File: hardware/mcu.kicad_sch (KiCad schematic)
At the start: 26 parts, among them SW1 BOOT / PTS810, SW2 RESET / PTS810, U2 ESP32-C6-MINI-1-H4, U4 BQ32000, Y1 32.768kHz

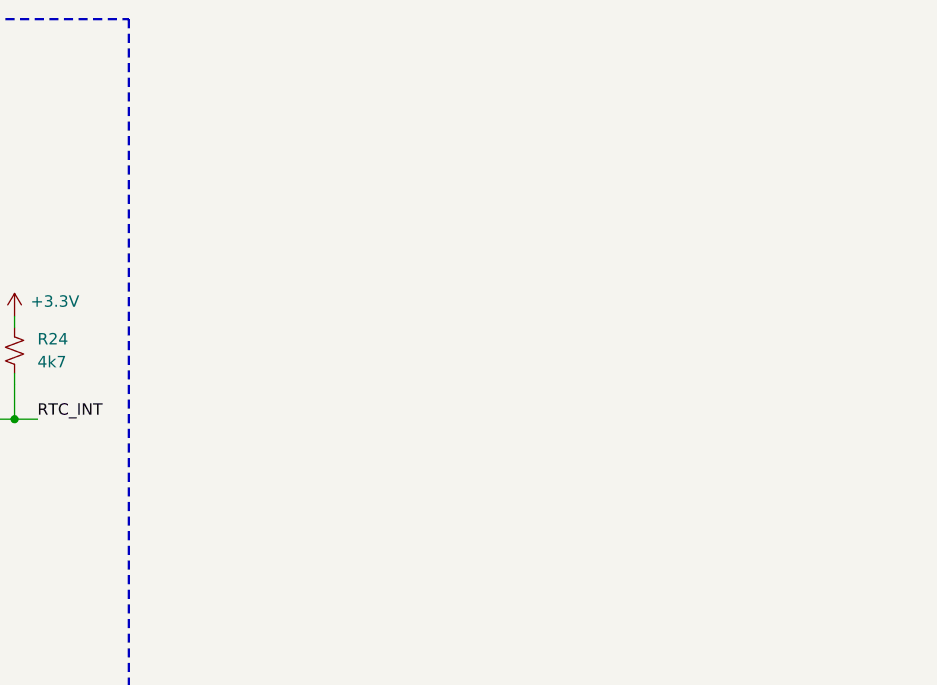
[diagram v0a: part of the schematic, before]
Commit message: hardware: I2C seviye dönüştürücüyü mcu'ya taşı, OUT_POS aktif deşarjı ekle (TASK-048/049/050)
- mcu: I2C seviye dönüştürücü (Q1, Q2, R4-R7) usb_pd_controller'dan
  taşındı; sayfa A4 -> A3. Bağlantı değişmedi.
- usb_pd_controller: R59 bleed yerine SW_EN kontrollü deşarj. Q4 BSS138P
  SW_EN'i ters çevirir, Q6 BSS138P OUT_POS'u R67 1k 2W 2512 üzerinden
  boşaltır; gate SW_OUT'tan R66 100k, D10 BZT52C12 ile 12 V. R59 10k 0805
  -> 100k 0603. Q1/Q2 alanları BSS138P,215 datasheet'ine göre düzeltildi.
- Karar: design_decisions/output/CIKIS_DESARJI_20260923.md; firmware
  deşarj bekleme ve dış kaynak uyarısı FIRMWARE_GEREKSINIMLERI.md §3.
- Backlog: TASK-048/049 Done, TASK-050 bring-up doğrulaması açıldı,
  TASK-006'ya footprint notu.

Kanıt: ERC 0/0. Netlist farkı yalnız beklenen netler: yeni DISCH_G
(D10.1, Q4.3, Q6.1, R66.2) ve Net-(Q6-D) (Q6.3, R67.2); SW_EN += Q4.1,
SW_OUT += R66.1, OUT_POS += R67.1, GND += D10.2, Q4.2, Q6.2.

Co-Authored-By: Claude Opus 5.5 <noreply@anthropic.com>
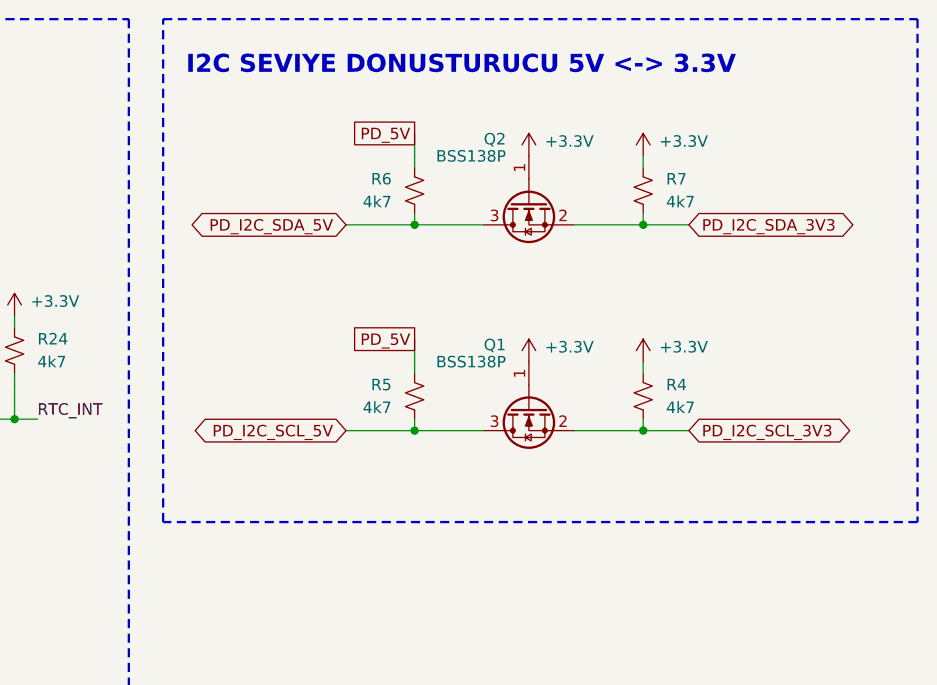
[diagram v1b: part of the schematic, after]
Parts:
- added Q1, Q2: BSS138P, Package_TO_SOT_SMD:SOT-23, symbol Transistor_FET:BSS138
- added R4, R5, R6, R7: 4k7, Resistor_SMD:R_0402_1005Metric, symbol Device:R_Small_US
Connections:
- net +3.3V: now also Q1.1 (G), Q2.1 (G), R4.2, R7.1
- net PD_I2C_SCL_3V3: now also Q1.2 (S), R4.1
- net PD_I2C_SDA_3V3: now also Q2.2 (S), R7.2
- new net PD_5V: R5.1, R6.1
- new net PD_I2C_SCL_5V: Q1.3 (D), R5.2
- new net PD_I2C_SDA_5V: Q2.3 (D), R6.2
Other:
- note added: "I2C SEVIYE DONUSTURUCU 5V <-> 3.3V"

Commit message: hardware: Ethernet mezanin blogu ve besleme anahtari (TASK-051/060)
Waveshare 2-CH UART TO ETH (CH9121) modulu mcu sayfasina mezanin olarak
baglandi. J8 (2x8) pinout'u ureticinin semasindan alindi; modulun 3V3
pinleri beslenir, AMS1117 atlanir, 5V bos. Kanal 1 UART0'a bagli
(GPIO16/17; loglar zaten USB-Serial/JTAG'de), CFG0 GPIO8'de (R37 10k
boot boyunca high tutar = normal mod), RUN yalniz TP14 pedinde.

Q8 TSM3443CX6 P-kanal yuksek-yan anahtari ETH_3V3'u keser: PD Fixed PDO
gecisindeki 2,5 W standby butcesinden modulun ~0,66 W'i dusulebiliyor.
ETH_PWR_EN = GPIO0, aktif-low; GPIO0 boot'ta yuksek empedans oldugu icin
R17 100k modulu kapali tutar. R16 22R -> 10k gate seri direnci, yeni C21
100n yumusak kalkis. RST1 baglanmadi: CH9121 0x02/0x0e ile yazilimdan
reset'lenebiliyor ve ayarlarini 0x0d ile EEPROM'da tuttugu icin guc
kesme yeniden yapilandirma gerektirmiyor.

Yeni proje sembolu Power_Supply_Custom:TSM3443CX6 (G=3, S=4, D pedleri
1/2/5/6 istifli). ERC 0 hata / 0 uyari, netlist 110 -> 120 net,
okunabilirlik denetimi degismedi. Analiz ve hesaplar:
design_decisions/output/ETHERNET_MODULU_ANALIZI_20260923.md

Co-Authored-By: Claude Opus 5 <noreply@anthropic.com>
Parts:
- added C10: 22u, Capacitor_SMD:C_0805_2012Metric, symbol Device:C
- added C20, C21: 100n, Capacitor_SMD:C_0402_1005Metric, symbol Device:C
- added J8: TBD, symbol Connector_Generic:Conn_02x08_Odd_Even
- added Q8: TSM3443CX6, Package_TO_SOT_SMD:SOT-23-6, symbol Power_Supply_Custom:TSM3443CX6
- added R17: 100k, Resistor_SMD:R_0402_1005Metric, symbol Device:R_Small_US
- added TP14: TestPoint, TestPoint:TestPoint_Pad_D1.0mm, symbol Connector:TestPoint
- R16: value 22R -> 10k; DesignNote TBD -> Q8 gate seri direnci. R17 100k ile bolucu: GPIO0 low iken g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; MPN RC0402FR-0722RP -> TC0250B1002TCC; SelectionNote Özdisan 839397; stok 4562 (21.09.2026); Uygun. -> R37/R10 ile ayni 10k 0402 (Ozdisan 569744).
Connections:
- net +3.3V: now also C21.1, Q8.4 (S), R17.1
- net GND: now also C10.2, C20.2, J8.11 (Pin_11), J8.12 (Pin_12)
- net UART_RX: now also J8.7 (Pin_7)
- net UART_TX: now also J8.5 (Pin_5)
- net ETH_CFG0: now reaches R15.2, TP9.1
- net ETH_CFG0: now also J8.3 (Pin_3)
- net ETH_PWR_EN: now reaches R16.1, TP10.1
- net ETH_PWR_EN: now also C21.2, Q8.3 (G), R17.2
- new net ETH_3V3: C10.1, C20.1, J8.13 (Pin_13), J8.14 (Pin_14), Q8.1 (D), Q8.2 (D), Q8.5 (D), Q8.6 (D)
- new net ETH_RUN: J8.4 (Pin_4), TP14.1
- no-connect marks 0 -> 8
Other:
- note added: "ETHERNET MEZANIN (CH9121) + BESLEME ANAHTARI"
- note added: "Waveshare 2-CH UART TO ETH (CH9121). Pin sirasi ureticinin semasindan (datasheets/2-CH_UART_TO_ETH_SCH.pdf); adim ve footprint numuneden (TASK-053). Besleme J8 3V3 pinlerinden: modulun AMS1117 5V->3V3 LDO'su atlanir, 5V bos. Q8 yuksek-yan anahtari PD Fixed PDO gecisinde modulu keser (~0,66 W). ETH_PWR_EN AKTIF-LOW (GPIO0 low = acik); GPIO0 float iken R17 kapali tutar. Kapatmadan once firmware GPI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"

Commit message: hardware: J8 Ethernet modulu footprint'i, 3D model ve PCB (TASK-054)
- Yeni kutuphane Module_Custom (fp-lib-table): Waveshare_2-CH_UART_TO_ETH.
  Standoff yok, 2x8 2.54 mm header + RJ45 tarafinda iki mekanik pin (MP,
  net yok) ile dogrudan lehim; RJ45 pim alaninda F.Cu keepout; courtyard
  RJ45'in 4.3 mm tasmasini kapsar. Olculer Waveshare olcu cizimi ve modul
  semasindan; mekanik pin konumu numuneyle dogrulanacak (TASK-053).
- Module_Custom.3dshapes: basitlestirilmis STEP (uretici model yayinlamiyor).
  Kaynak: .claude/skills/kicad-footprint/examples/waveshare_2ch_uart_to_eth.py
- mcu: J8 Footprint atandi, Value TBD -> 2-CH UART TO ETH, Manufacturer/
  Pitch/Height/SelectionNote (SAMM MP02965)/AssemblyNote. Netlist degismedi,
  ERC 0/0.
- PCB: J8 eklendi (update_pcb --keep-tracks), 3D model bagli; DRC schematic
  parity 1 -> 0. pcbnew kaydi karttaki metinlere (thickness ...) ekledi
  (~2500 satir, bicim normalizasyonu, baglanti degisikligi yok).
- CHANGES.TXT guncellendi.

Co-Authored-By: Claude Opus 5.5 <noreply@anthropic.com>
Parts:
- J8: value TBD -> 2-CH UART TO ETH; footprint (none) -> Module_Custom:Waveshare_2-CH_UART_TO_ETH; AssemblyNote TBD -> Standoff yok, dogrudan lehim. P2/P3 mekanik pinleri MP pedl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; Height TBD -> ~17.5 mm (2.5 header ara parcasi + 15.0 RJ45); Manufacturer TBD -> Waveshare; Orientation TBD -> Vertical; Package TBD -> Modul 53 x 22 mm, 2x8 THT header + 2 mekanik pin; Pitch TBD -> 2.54 mm; SelectionNote Adim (2,54 mm varsayimi) ve footprint numune ile kesinlesec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 -> SAMM Market MP02965; 634,89 TL + KDV; stok 19 (23.09.2026).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
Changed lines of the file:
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@@
 			)
 		)
-		(property "Value" "TBD"
+		(property "Value" "2-CH UART TO ETH"
 			(at 107.95 184.15 0)
 			(show_name no)
@@
 			)
 		)
-		(property "Footprint" ""
+		(property "Footprint" "Module_Custom:Waveshare_2-CH_UART_TO_ETH"
 			(at 109.22 195.58 0)
 			(hide yes)
@@
 			)
 		)
-		(property "Description" "Waveshare 2-CH UART TO ETH (CH9121) mezanin header 2x8"
+		(property "Description" "Waveshare 2-CH UART TO ETH (CH9121) modulu, 2x8 header ile ana karta dogrudan lehimli"
 			(at 109.22 195.58 0)
 			(hide yes)
@@
 			)
 		)
-		(property "Manufacturer" "TBD"
+		(property "Manufacturer" "Waveshare"
 			(at 109.22 195.58 0)
 			(hide yes)
@@
 			)
 		)
-		(property "Package" "TBD"
+		(property "Package" "Modul 53 x 22 mm, 2x8 THT header + 2 mekanik pin"
 			(at 109.22 195.58 0)
 			(hide yes)
@@
 			)
 		)
-		(property "Height" "TBD"
+		(property "Height" "~17.5 mm (2.5 header ara parcasi + 15.0 RJ45)"
 			(at 109.22 195.58 0)
 			(hide yes)
@@
 			)
 		)
-		(property "SelectionNote" "Adim (2,54 mm varsayimi) ve footprint numune ile kesinlesecek (TASK-053)."
-			(at 109.22 195.58 0)
-			(hide yes)
-			(show_name no)
-			(do_not_autoplace no)
-			(effects
-				(font
-					(size 1.27 1.27)
-				)
-			)
-		)
-		(property "AssemblyNote" "TBD"
+		(property "SelectionNote" "SAMM Market MP02965; 634,89 TL + KDV; stok 19 (23.09.2026). Footprint Waveshare olcu cizimiyle cizildi; mekanik pin konumu numuneyle dogrulanacak (TASK-053)."
+			(at 109.22 195.58 0)
+			(hide yes)
+			(show_name no)
+			(do_not_autoplace no)
+			(effects
+				(font
+					(size 1.27 1.27)
+				)
+			)
+		)
+		(property "AssemblyNote" "Standoff yok, dogrudan lehim. P2/P3 mekanik pinleri MP pedlerine lehimlenir (net yok). Header pinleri kart altindan ~4.4 mm cikar. RJ45 kart kenarindan 4.3 mm tasar."
 			(at 109.22 195.58 0)
 			(hide yes)
@@
 			)
 		)
-		(property "Pitch" "TBD"
+		(property "Pitch" "2.54 mm"
 			(at 109.22 195.58 0)
 			(hide yes)
@@
 			)
 		)
-		(property "Orientation" "TBD"
-			(at 109.22 195.58 0)
-			(hide yes)
+		(property "Orientation" "Vertical"
+			(at 109.22 195.58 0)
+			(hide yes)

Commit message: REV_C yerlesim: agirlikli ratsnest araclari, FPC keepout, routability ve ESP32 pin atamasi
Yerlesim (hardware/gopo.kicad_pcb, kilitli H1-H4/J3 yerinde, parite 0):
- TASK-115: kilitsiz parcalarin agirlikli ratsnest ile sifirdan yerlesimi
- TASK-118: agirlik 10/5/5 (W_ORDINARY) ve LCD FPC bukum yolunda top'ta parca yok
- TASK-119: kesisme cezasi, dekuplaj-IC ayni yuz kurali (flip destegi), IC-yerel kenarlar
- TASK-122: In2 guc polygonlari metrige yansidi (PLANE_NETS), sinyal kesismesi 75 -> 51
- TASK-124: BOOST LNS (sicak dongu sabit), C23 SS 7.0 -> 2.7 mm; PD degismedi

ESP32-C6 pin atamasi (TASK-123, kullanici onayli):
- mcu.kicad_sch: U2 pinlerindeki 12 etiket yeniden adlandirildi; ERC 0, netlist
  farki yalniz bu netler. Sinyal kesismesi 51 -> 38.
- FIRMWARE_GEREKSINIMLERI.md pin tablosu; TASK-033 I2C GPIO22/23.

Araclar:
- kicad-placement skill: placelib/place.py (anneal/legal/refine/sweep/untangle/align,
  LNS --blocks), pcb_dump/apply/check/render, pcb_freeroute (TASK-120 deneme routing)
- update_pcb.py: board-only ve kilitli footprint'ler artik silinmiyor (H1-H4, MECH_ENC)

Kararlar: design_decisions/output/SIFIRDAN_YERLESIM_AGIRLIKLI_RATSNEST_20260929.md
Acik isler: TASK-116 (serigrafi), TASK-117, TASK-121.

Co-Authored-By: Claude Opus 5.5 <noreply@anthropic.com>
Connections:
- net ENCODER_A: now also U2.6 (IO3); no longer U2.28 (IO22)
- net ENCODER_B: now also U2.16 (IO7); no longer U2.29 (IO23)
- net ENCODER_SW: now also U2.19 (IO14); no longer U2.27 (IO21)
- net INA_ALERT: now also U2.26 (IO20); no longer U2.6 (IO3)
- net PD_I2C_SCL_3V3: now also U2.28 (IO22); no longer U2.24 (IO18)
- net PD_I2C_SDA_3V3: now also U2.29 (IO23); no longer U2.25 (IO19)
- net PD_INT_3V3: now also U2.5 (IO2); no longer U2.26 (IO20)
- net RTC_INT: now also U2.27 (IO21); no longer U2.5 (IO2)
- net TFT_CS: now also U2.20 (IO15); no longer U2.19 (IO14)
- net TFT_DC: now also U2.10 (IO5); no longer U2.16 (IO7)
- net TFT_MOSI: now also U2.24 (IO18); no longer U2.10 (IO5)
- net TFT_RST: now also U2.25 (IO19); no longer U2.20 (IO15)
